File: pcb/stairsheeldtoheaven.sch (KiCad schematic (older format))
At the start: 26 parts, among them P1 CONN_10X2, P10 5, P11 6, P12 7, P13 8, P14 9, P15 10, P16 11, P17 12, P18 13, P19 14, P2 LED1, P20 15, P21 16, P22 17, P23 18, P24 19, P25 20, P4 5V, P5 1, P6 2, P7 3, P8 4, P9 12V

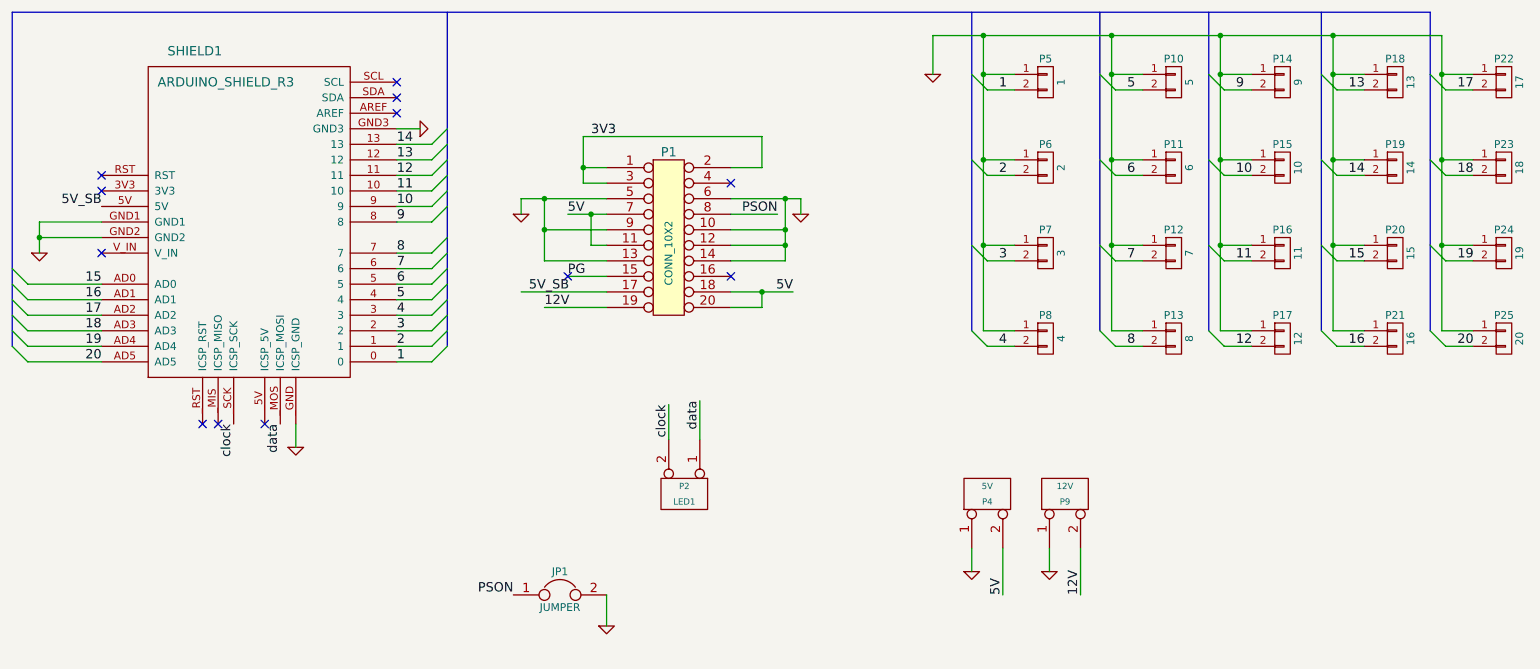
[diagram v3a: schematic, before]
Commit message: Ajout pin PowerGood redefinition plan de masse regénération fichiers de fabrication
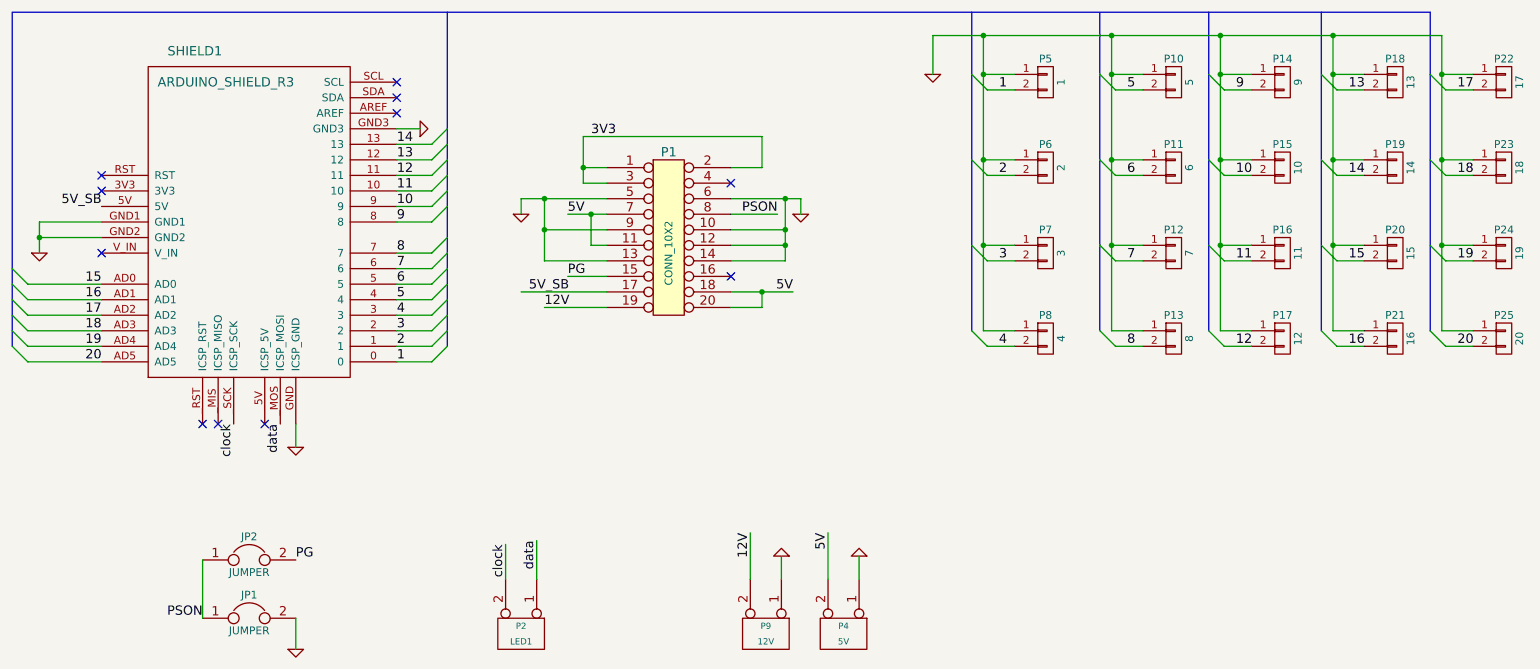
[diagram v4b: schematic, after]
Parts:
- added JP2: JUMPER, Pin_Headers:Pin_Header_Straight_1x02, symbol JUMPER
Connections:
- net PG: now also JP2.2
- net PSON: now also JP2.1
- no-connect marks 12 -> 11
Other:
- moved on the sheet: JP1, P2, P4, P9
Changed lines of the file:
@@
 L JUMPER JP1
 U 1 1 561441BD
-P 4450 4600
-F 0 "JP1" H 4450 4750 50  0000 C CNN
-F 1 "JUMPER" H 4450 4520 50  0000 C CNN
-F 2 "Pin_Headers:Pin_Header_Straight_1x02" H 4450 4600 60  0001 C CNN
-F 3 "" H 4450 4600 60  0000 C CNN
-	1    4450 4600
+P 2450 4750
+F 0 "JP1" H 2450 4900 50  0000 C CNN
+F 1 "JUMPER" H 2450 4670 50  0000 C CNN
+F 2 "Pin_Headers:Pin_Header_Straight_1x02" H 2450 4750 60  0001 C CNN
+F 3 "" H 2450 4750 60  0000 C CNN
+	1    2450 4750
 	1    0    0    -1
 $EndComp
@@
 L CONN_2 P4
 U 1 1 56144C11
-P 7200 3950
-F 0 "P4" V 7150 3950 40  0000 C CNN
-F 1 "5V" V 7250 3950 40  0000 C CNN
-F 2 "Connect:bornier2" H 7200 3950 60  0001 C CNN
-F 3 "" H 7200 3950 60  0000 C CNN
-	1    7200 3950
-	0    -1   -1   0
+P 6275 4850
+F 0 "P4" V 6225 4850 40  0000 C CNN
+F 1 "5V" V 6325 4850 40  0000 C CNN
+F 2 "Connect:bornier2" H 6275 4850 60  0001 C CNN
+F 3 "" H 6275 4850 60  0000 C CNN
+	1    6275 4850
+	0    1    1    0
 $EndComp
 $Comp
 L CONN_2 P9
 U 1 1 56144C12
-P 7700 3950
-F 0 "P9" V 7650 3950 40  0000 C CNN
-F 1 "12V" V 7750 3950 40  0000 C CNN
-F 2 "Connect:bornier2" H 7700 3950 60  0001 C CNN
-F 3 "" H 7700 3950 60  0000 C CNN
-	1    7700 3950
-	0    -1   -1   0
+P 5775 4850
+F 0 "P9" V 5725 4850 40  0000 C CNN
+F 1 "12V" V 5825 4850 40  0000 C CNN
+F 2 "Connect:bornier2" H 5775 4850 60  0001 C CNN
+F 3 "" H 5775 4850 60  0000 C CNN
+	1    5775 4850
+	0    1    1    0
 $EndComp
 Text Label 4650 1650 0    60   ~ 0
@@
 Text Label 4350 2750 0    60   ~ 0
 12V
-Text Label 7800 4600 1    60   ~ 0
+Text Label 5675 4200 3    60   ~ 0
 12V
-Text Label 7300 4600 1    60   ~ 0
+Text Label 6175 4200 3    60   ~ 0
 5V
 $Comp
 L GND-RESCUE-atxpowerboard #PWR03
 U 1 1 56144C18
-P 7600 4450
-F 0 "#PWR03" H 7600 4450 30  0001 C CNN
-F 1 "GND" H 7600 4380 30  0001 C CNN
-F 2 "" H 7600 4450 60  0000 C CNN
-F 3 "" H 7600 4450 60  0000 C CNN
-	1    7600 4450
-	1    0    0    -1
+P 5875 4350
+F 0 "#PWR03" H 5875 4350 30  0001 C CNN
+F 1 "GND" H 5875 4280 30  0001 C CNN
+F 2 "" H 5875 4350 60  0000 C CNN
+F 3 "" H 5875 4350 60  0000 C CNN
+	1    5875 4350
+	-1   0    0    1
 $EndComp
 $Comp
 L GND-RESCUE-atxpowerboard #PWR04
 U 1 1 56144C19
-P 7100 4450
-F 0 "#PWR04" H 7100 4450 30  0001 C CNN
-F 1 "GND" H 7100 4380 30  0001 C CNN
-F 2 "" H 7100 4450 60  0000 C CNN
-F 3 "" H 7100 4450 60  0000 C CNN
-	1    7100 4450
-	1    0    0    -1
+P 6375 4350
+F 0 "#PWR04" H 6375 4350 30  0001 C CNN
+F 1 "GND" H 6375 4280 30  0001 C CNN
+F 2 "" H 6375 4350 60  0000 C CNN
+F 3 "" H 6375 4350 60  0000 C CNN
+	1    6375 4350
+	-1   0    0    1
 $EndComp
 $Comp
@@
 Text Label 10225 3000 0    60   ~ 0
 20
-Text Label 4150 4600 2    60   ~ 0
+Text Label 2150 4750 2    60   ~ 0
 PSON
 $Comp
 L GND-RESCUE-atxpowerboard #PWR05
 U 1 1 561498D7
-P 4750 4800
-F 0 "#PWR05" H 4750 4800 30  0001 C CNN
-F 1 "GND" H 4750 4730 30  0001 C CNN
-F 2 "" H 4750 4800 60  0000 C CNN
-F 3 "" H 4750 4800 60  0000 C CNN
-	1    4750 4800
+P 2750 4950
+F 0 "#PWR05" H 2750 4950 30  0001 C CNN
+F 1 "GND" H 2750 4880 30  0001 C CNN
+F 2 "" H 2750 4950 60  0000 C CNN
+F 3 "" H 2750 4950 60  0000 C CNN
+	1    2750 4950
 	1    0    0    -1
 $EndComp
@@
 L CONN_2 P2
 U 1 1 5614A0FA
-P 5250 3950
-F 0 "P2" V 5200 3950 40  0000 C CNN
-F 1 "LED1" V 5300 3950 40  0000 C CNN
-F 2 "Connect:bornier2" H 5250 3950 60  0001 C CNN
-F 3 "" H 5250 3950 60  0000 C CNN
-	1    5250 3950
+P 4200 4850
+F 0 "P2" V 4150 4850 40  0000 C CNN
+F 1 "LED1" V 4250 4850 40  0000 C CNN
+F 2 "Connect:bornier2" H 4200 4850 60  0001 C CNN
+F 3 "" H 4200 4850 60  0000 C CNN
+	1    4200 4850
 	0    1    1    0
 $EndComp
-Text Label 5350 3350 3    60   ~ 0
+Text Label 4300 4250 3    60   ~ 0
 data
-Text Label 5150 3375 3    60   ~ 0
+Text Label 4100 4275 3    60   ~ 0
 clock
 Text Label 2650 3500 3    60   ~ 0
@@
 	4750 2750 4350 2750
 Wire Wire Line
-	7800 4300 7800 4600
-Wire Wire Line
-	7300 4300 7300 4600
-Wire Wire Line
-	7600 4300 7600 4450
-Wire Wire Line
-	7100 4450 7100 4300
+	5675 4500 5675 4200
+Wire Wire Line
+	6175 4500 6175 4200
+Wire Wire Line
+	5875 4500 5875 4350
+Wire Wire Line
+	6375 4350 6375 4500
 Wire Wire Line
 	5750 2750 5750 2650
@@
 	10150 3000 10325 3000
 Wire Wire Line
-	4750 4600 4750 4800
+	2750 4750 2750 4950
 Wire Wire Line
 	1500 2200 1100 2200
@@
 Connection ~ 1100 2300
 Wire Wire Line
-	5350 3600 5350 3350
+	4300 4500 4300 4250
 Wire Wire Line
 	2750 3500 2750 3650
@@
 NoConn ~ 3400 1400
 NoConn ~ 3400 1300
-NoConn ~ 4500 2550
 $Comp
 L GND-RESCUE-atxpowerboard #PWR09
@@
 	3400 1600 3550 1600
 Wire Wire Line
-	5150 3600 5150 3375
+	4100 4500 4100 4275
+$Comp
+L JUMPER JP2
+U 1 1 5616612B
+P 2450 4375
+F 0 "JP2" H 2450 4525 50  0000 C CNN
+F 1 "JUMPER" H 2450 4295 50  0000 C CNN
+F 2 "Pin_Headers:Pin_Header_Straight_1x02" H 2450 4375 60  0001 C CNN
+F 3 "" H 2450 4375 60  0000 C CNN
+	1    2450 4375
+	1    0    0    -1
+$EndComp
+Text Label 2750 4375 0    60   ~ 0
+PG
+Wire Wire Line
+	2150 4375 2150 4750
 $EndSCHEMATC
